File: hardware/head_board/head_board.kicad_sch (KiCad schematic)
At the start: 3 parts

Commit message: v1 revision to the schematic
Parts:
- removed H1, H2, H3: GND, MountingHole:MountingHole_3mm_Pad, symbol Mechanical:MountingHole_Pad
- added H? (x3): GND, MountingHole:MountingHole_3mm_Pad, symbol Mechanical:MountingHole_Pad
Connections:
- net GND: now also H?.1, H?.1, H?.1
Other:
- sheet MCU renamed Microcontroller
- removed sheet Outputs
- sheet Connections ports: added AUX_OUT, QWIIC_SCL, QWIIC_SDA; removed none
- sheet Microcontroller ports: added AUX_OUT, QWIIC_SCL, QWIIC_SDA; removed none
- note added: "Mounting holes"
- title: Candela (head) -> Candela Head

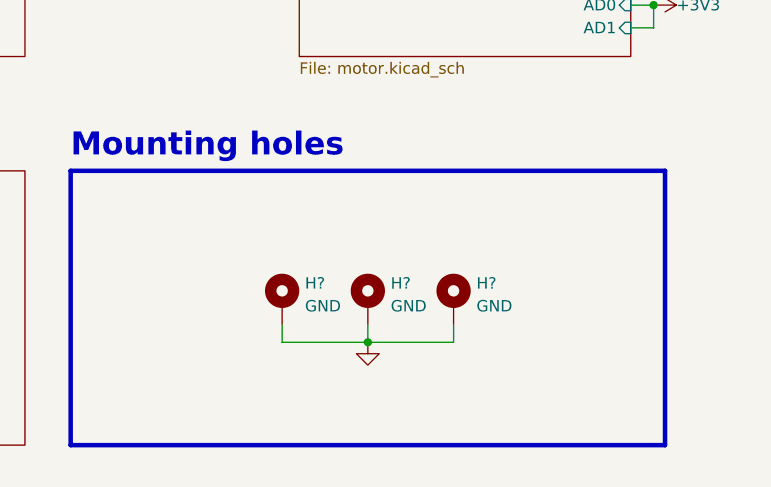
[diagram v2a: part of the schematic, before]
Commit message: Footprints assigned
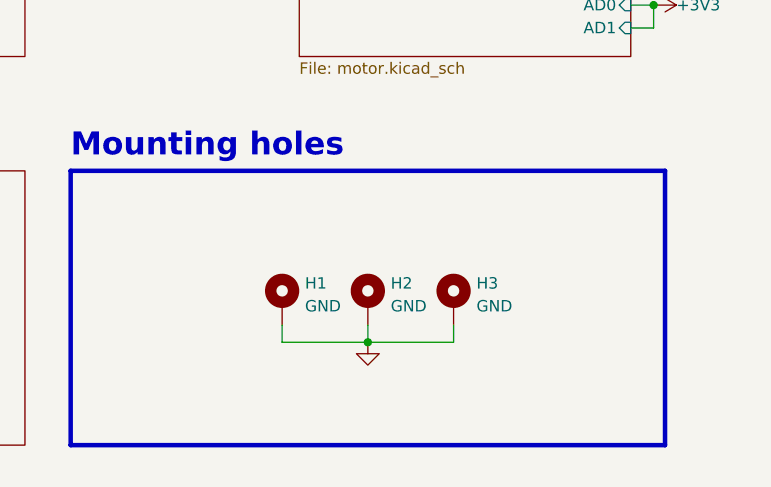
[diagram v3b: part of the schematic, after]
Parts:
- gave numbers to parts that had none: 3

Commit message: V2 of the head board (Jellyfish)
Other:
- sheet Connections ports: added BLTOUCH_CONTROL, BLTOUCH_OUT, IN_1, IN_2; removed none
- sheet Microcontroller ports: added BLTOUCH_CONTROL, BLTOUCH_STATUS, IN_1, IN_2; removed none
- title: Candela Head -> Jellyfish

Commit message: V1 of the tailboard
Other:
- title: Jellyfish -> Candela Head
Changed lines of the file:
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@@
   (paper "USLetter")
   (title_block
-    (title "Jellyfish")
-    (date "2022-09-07")
-    (rev "v2")
+    (title "Candela Head")
+    (date "2022-07-27")
+    (rev "v1")
     (company "Winterbloom")
     (comment 1 "Alethea Flowers")
     (comment 2 "CERN-OHL-P V2")
-    (comment 3 "jellyfish.wntr.dev")
   )
   (junction (at 121.92 186.69) (diameter 0) (color 0 0 0 0)
